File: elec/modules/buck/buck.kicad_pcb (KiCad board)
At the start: 2 copper layers, 30.5 x 40.6 mm, 28 parts, among them J1 Conn_01x08, J2 Conn_01x08, U2 TPS5430DDA, U2 TPS5430DDAG4, U3 TPS5430DDAG4

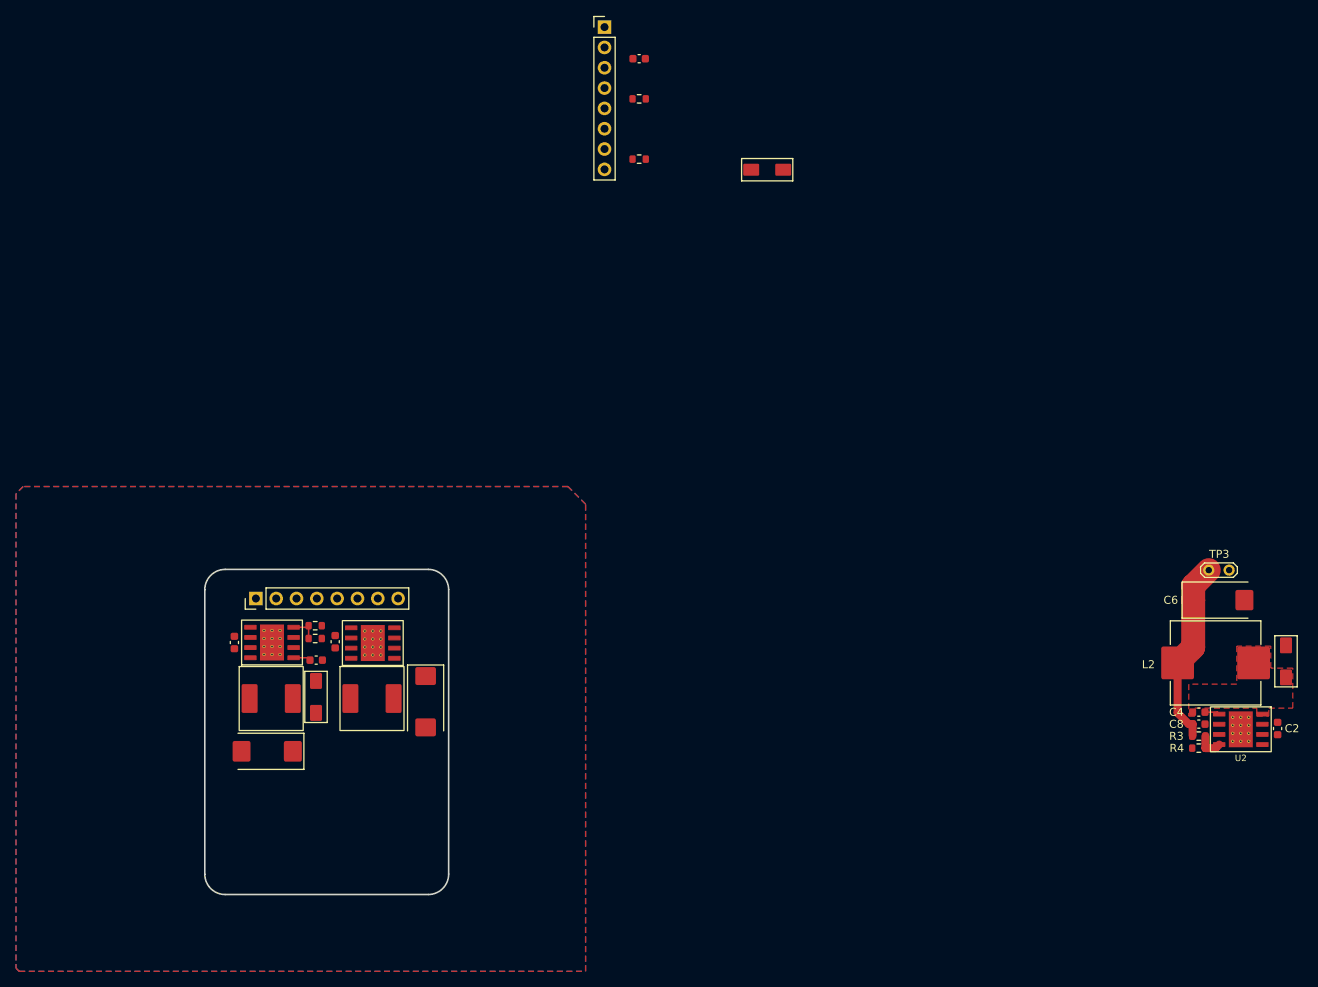
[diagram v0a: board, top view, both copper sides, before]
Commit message: added fusion fat module
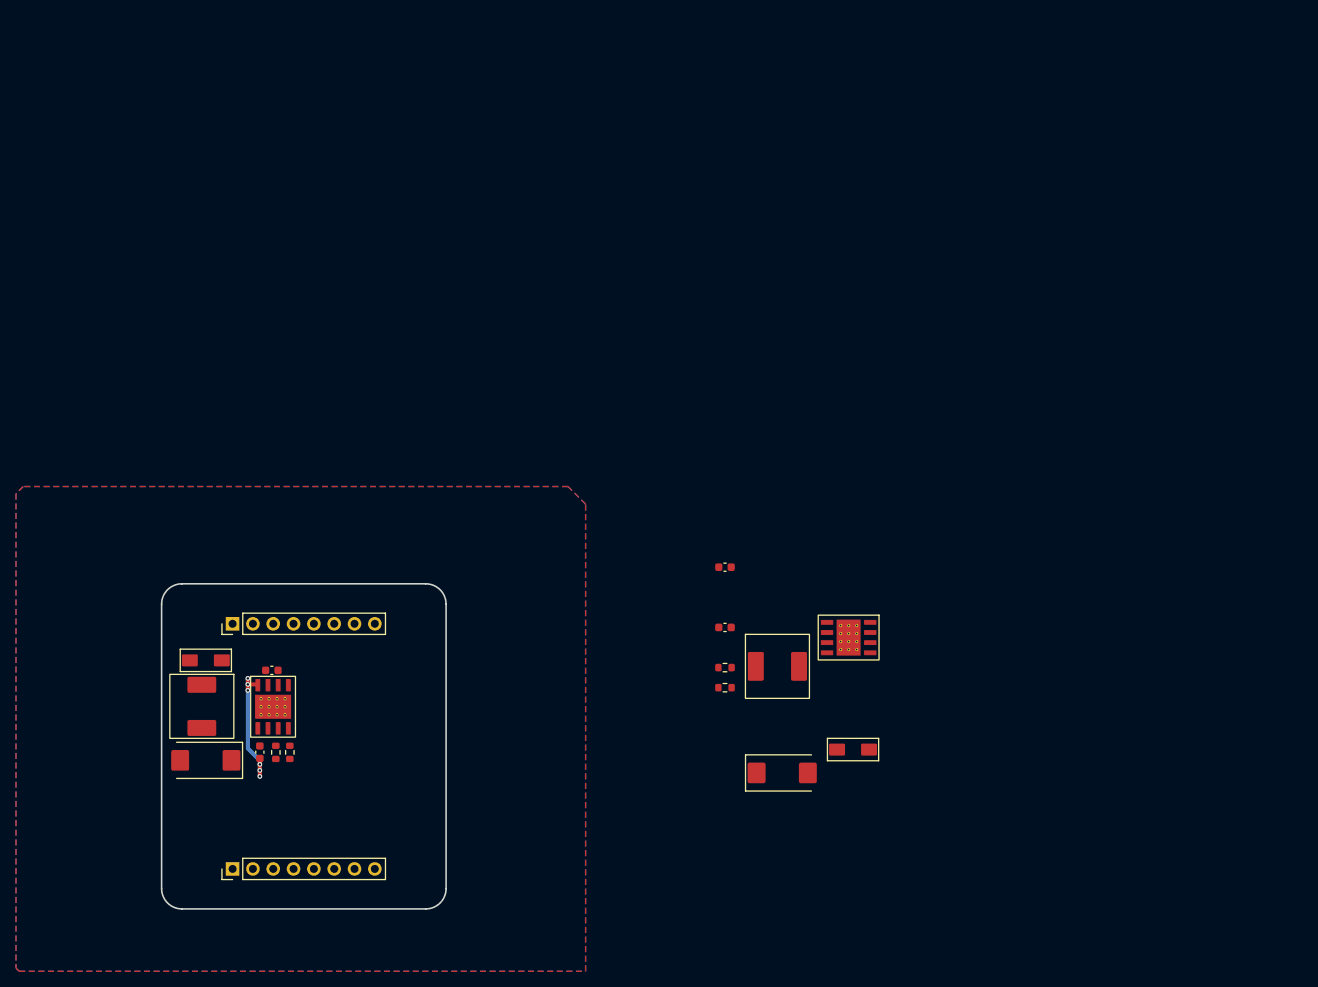
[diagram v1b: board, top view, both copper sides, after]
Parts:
- removed the C2 at (140.2, 78.7)
- removed the C2 at (258.0, 89.5)
- removed C4: 10n, Capacitor_SMD:C_0603_1608Metric
- removed the C6 at (137.8, 81.0)
- removed the C6 at (250.7, 73.5)
- removed the C8 at (248.2, 89.0)
- removed the C8 at (131.7, 92.4)
- removed the D2 at (137.8, 85.6)
- removed the D2 at (259.1, 81.2)
- removed the L2 at (250.2, 81.3)
- removed the L2 at (132.2, 85.8)
- removed R3: 10K, Resistor_SMD:R_0603_1608Metric
- removed R4: 3K24, Resistor_SMD:R_0603_1608Metric
- removed TP3: TestPoint_2Pole, TestPoint:TestPoint_2Pads_Pitch2.54mm_Drill0.8mm
- removed the U2 at (253.4, 89.7)
- removed the U2 at (144.9, 78.9)
- added C2: 10u, Capacitor_SMD:C_0603_1608Metric, F.Cu at (132.3, 82.3)
- added C6: 10n, Capacitor_SMD:C_0603_1608Metric, F.Cu at (188.9, 76.9)
- added C8: 220u, Capacitor_Tantalum_SMD:CP_EIA-7343-15_Kemet-W_HandSolder, F.Cu at (196.1, 95.1)
- added D2: SS54, Buckies:DIOM5025X220N, F.Cu at (204.9, 92.2)
- added L2: 15uH, Buckies:0630 One Piece Inductor, F.Cu at (195.5, 81.8)
- added U2: TPS5430DDAG4, Buckies:TI_SO-PowerPAD-8, F.Cu at (132.4, 86.8)
- moved J2 115.0 mm to (127.4, 107.1), turned to 90 degrees
- moved C3 98.8 mm to (130.8, 92.5), turned to -90 degrees
- moved R10 93.5 mm to (132.8, 92.5), turned to 90 degrees
- moved D1 93.2 mm to (124.0, 81.0), turned to 180 degrees
- moved R37 86.1 mm to (134.5, 92.5), turned to -90 degrees
- moved U3 72.1 mm to (204.4, 78.2), turned to 0 degrees
- moved C1 62.0 mm to (188.9, 69.4), turned to 0 degrees
- moved R28 51.6 mm to (188.9, 84.4), turned to 0 degrees
- moved R11 51.5 mm to (188.9, 81.9)
- moved C5 28.4 mm to (124.0, 93.5), turned to 180 degrees
- moved L1 21.3 mm to (123.5, 86.8), turned to -90 degrees
- moved J1 4.30 mm to (127.4, 76.5)
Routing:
- net +5V: track 23.4 -> 0.00 mm
- net Net-(D1-K): track 0.00 -> 17.9 mm, vias 0 -> 6
- net Net-(U3-VSENSE): track 3.56 -> 0.00 mm
- net Net-(U2-VSENSE): track 3.41 -> 0.00 mm
- net Net-(U3-BOOT): track 2.17 -> 0.00 mm
- net Net-(U2-BOOT): track 1.88 -> 0.00 mm
- removed copper zone on F.Cu, net Net-(D2-K)
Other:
- board size 30.5 x 40.6 mm -> 35.6 x 40.6 mm

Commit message: moving somethings
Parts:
- moved L1 1.00 mm to (124.5, 86.8)
- moved D1 0.75 mm to (124.8, 81.0)
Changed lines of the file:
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@@
 	(footprint "Buckies:0630 One Piece Inductor"
 		(layer "F.Cu")
-		(at 123.53 86.779999 -90)
+		(at 124.53 86.779999 -90)
 		(property "Reference" "L1"
 			(at 0 0 270)
@@
 	(footprint "Buckies:DIOM5025X220N"
 		(layer "F.Cu")
-		(at 124.03 81.029999 180)
+		(at 124.78 81.029999 180)
 		(descr "SMA (DO-214AC)")
 		(tags "Schottky Diode")

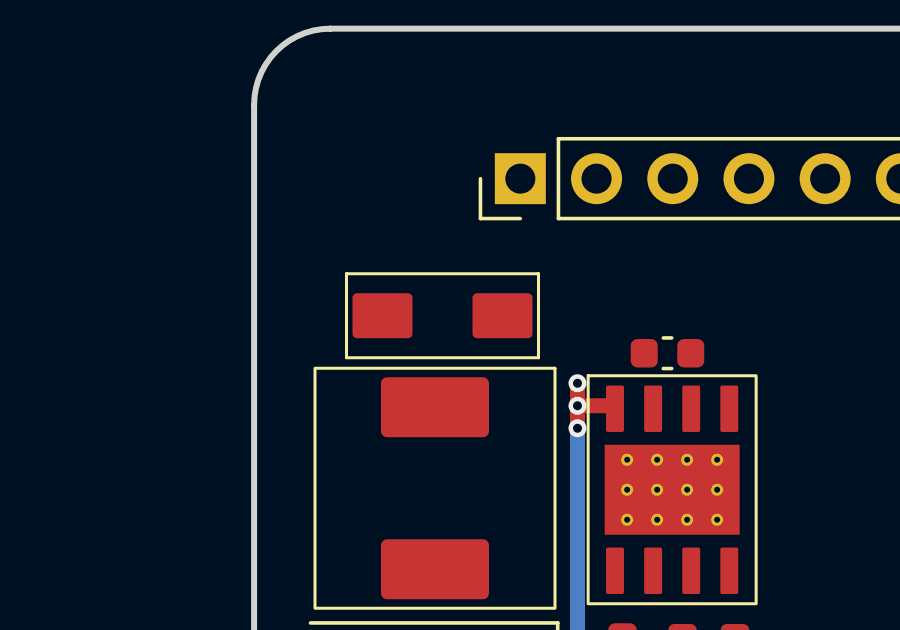
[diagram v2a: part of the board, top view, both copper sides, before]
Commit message: fix: edited buck
moved a singular tantulum by a few mm
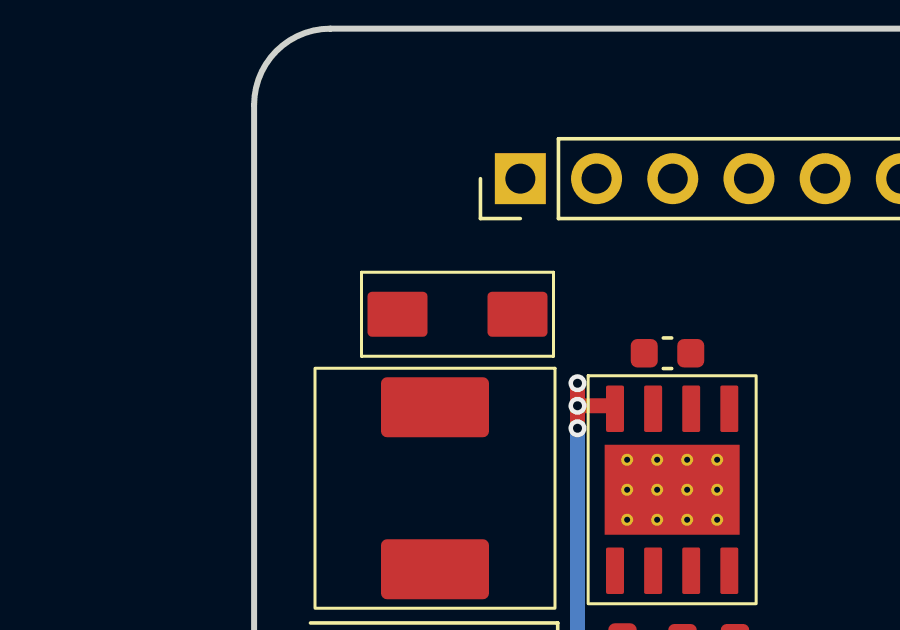
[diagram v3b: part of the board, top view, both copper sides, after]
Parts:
- moved D1 0.50 mm to (125.3, 81.0)
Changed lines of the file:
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@@
 	(footprint "Buckies:DIOM5025X220N"
 		(layer "F.Cu")
-		(at 124.78 81.029999 180)
+		(at 125.28 80.979999 180)
 		(descr "SMA (DO-214AC)")
 		(tags "Schottky Diode")

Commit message: did buck +3d models_ the actual buck er 3d mode'
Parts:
- moved D2 63.5 mm to (142.0, 83.2), turned to 180 degrees
- moved U3 56.4 mm to (149.0, 89.1), turned to 90 degrees
- moved C8 55.3 mm to (140.8, 95.8), turned to 180 degrees
- moved L2 54.7 mm to (141.3, 89.0), turned to -90 degrees
- moved C6 45.5 mm to (147.0, 94.8), turned to -90 degrees
- moved C1 42.6 mm to (149.0, 84.3)
- moved R28 41.0 mm to (149.3, 94.8), turned to 90 degrees
- moved R11 40.0 mm to (151.0, 94.8), turned to -90 degrees
- moved C2 2.14 mm to (133.0, 84.3)
- moved C3 2.14 mm to (131.5, 94.5)
- moved C5 2.14 mm to (124.8, 95.5)
- moved D1 2.14 mm to (126.0, 83.0)
- moved L1 2.14 mm to (125.3, 88.8)
- moved R10 2.14 mm to (133.5, 94.5)
- moved R37 2.14 mm to (135.3, 94.5)
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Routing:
- net Net-(D2-K): track 0.00 -> 10.6 mm
- net Net-(D1-K): track 17.9 -> 11.1 mm, vias 6 -> 0
- net Net-(U2-VSENSE): track 0.00 -> 4.00 mm
- net Net-(U3-VSENSE): track 0.00 -> 3.96 mm
- net Net-(U2-BOOT): track 0.00 -> 2.30 mm
- net Net-(U3-BOOT): track 0.00 -> 2.24 mm
- added copper zone on F.Cu, net +12V
- added copper zone on F.Cu, net +3V3
- added copper zone on F.Cu, net +5V
- added copper zone on F.Cu, net Net-(D1-K)
- added copper zone on F.Cu, net Net-(D2-K)
